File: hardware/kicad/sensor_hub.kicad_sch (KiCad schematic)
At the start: 59 parts, among them J1 5-1634500-1, J2 Wago-DS18B20, J3 Wago-DHT22, J4 Wago-PIR, J5 Wago-GP16, J6 Wago-GP17, J7 Wago-Relay, J8 Phoenix-EC4pin, J9 Phoenix-Power, K1 SRD-05VDC-SL-C, Q1 BC817-40, Q2 BSS84PXUMA1, U1 PicoW, U2 ADS1115IDGSR, U3 LMP91200SD/NOPB, U4 AD8603ARTZ-R2, U5 AP2112K-3.3TRG1, U6 VEML7700-TT

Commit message: hardware: 230 VAC relay spec + sync schematic with docs
- Relays switched to Omron G2RL-1-E (reinforced coil-contact insulation)
  for 230 VAC / 5 A per channel; 8 mm SELV-MAINS creepage/clearance,
  isolation slot, MAINS zone keepout, 3 mm mains traces, X2 snubbers
- Schematic: add K2, Q3, R18, D3, R19/C19, R20/C20, J10 (W7); drop R4
  and second 10M on pH input; renumber pull-ups to one ref per function;
  fix symbol/footprint names for KiCad 10; upgrade file to KiCad 10
- Add project symbol library with VEML7700
- schematic.md gets a master reference designator list; BOM and
  footprints.md aligned; AP2112K fed from VSYS

Co-Authored-By: Claude Opus 5.5 <noreply@anthropic.com>
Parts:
- removed R12, R13, R14: 1k, Resistor_SMD:R_0603_1608Metric, symbol Device:R
- removed R2: 10M, Resistor_SMD:R_0603_1608Metric, symbol Device:R
- removed R22: 10k, Resistor_SMD:R_0603_1608Metric, symbol Device:R
- removed R5, R6: 100k, Resistor_SMD:R_0603_1608Metric, symbol Device:R
- added C19, C20: 100nF X2 275VAC, symbol Device:C
- added D3: 1N4148W, Diode_SMD:D_SOD-123, symbol Device:D
- added J10: Wago-Relay2, symbol Connector_Generic:Conn_01x03
- added K2: G2RL-1-E DC5, Relay_THT:Relay_SPDT_Omron_G2RL-1-E, symbol Relay:G2RL-1-E
- added Q3: BC817-40, Package_TO_SOT_SMD:SOT-23, symbol Transistor_BJT:BC817
- added R18: 1k, Resistor_SMD:R_0603_1608Metric, symbol Device:R
- added R19, R20: 100R, Resistor_SMD:R_1206_3216Metric, symbol Device:R
- J1: footprint Connector_Coaxial:BNC_TE-Connectivity_1-1634500-1_Horizontal -> (none); symbol Connector_Coaxial:BNC_Jack -> Connector:Conn_Coaxial
- J2, J3, J4, J5, J6: footprint TerminalBlock_Wago:TerminalBlock_Wago_2060-453_1x03_P5.00mm_Horizontal -> (none)
- J7: value Wago-Relay -> Wago-Relay1; footprint TerminalBlock_Wago:TerminalBlock_Wago_2060-453_1x03_P5.00mm_Horizontal -> (none)
- J8: footprint TerminalBlock_Phoenix:TerminalBlock_Phoenix_PT-1,5_4-3,5-H_1x04_P3.50mm_Horizontal -> TerminalBlock_Phoenix:TerminalBlock_Phoenix_PT-1,5-4-3.5-H_1x04_P3.50mm_Horizontal
- J9: footprint TerminalBlock_Phoenix:TerminalBlock_Phoenix_PT-1,5_2-5,0-H_1x02_P5.00mm_Horizontal -> TerminalBlock_Phoenix:TerminalBlock_Phoenix_PT-1,5-2-5.0-H_1x02_P5.00mm_Horizontal
- K1: value SRD-05VDC-SL-C -> G2RL-1-E DC5; footprint Relay_THT:Relay_SPDT_Songle_SRD-xxVDC-SL-C -> Relay_THT:Relay_SPDT_Omron_G2RL-1-E; symbol Device:Relay_SPDT -> Relay:G2RL-1-E
- R5: renamed from R19; value 10k -> 4k7
- U1: value PicoW -> Pico W; footprint MicrocontrollerBoard:RaspberryPi_PicoW -> Module:RaspberryPi_Pico_W_SMD; symbol MCU_RaspberryPi_RP2040:RaspberryPi_PicoW -> MCU_Module:RaspberryPi_Pico_W
- U2: footprint Package_SO:VSSOP-10_3x3mm_P0.5mm -> Package_SO:MSOP-10_3x3mm_P0.5mm; symbol Analog_ADC:ADS1115xDGS -> Analog_ADC:ADS1115IDGS
- U3: footprint Package_SO:SOIC-14_3.9x8.65mm_P1.27mm -> Package_SO:SOIC-14_3.9x8.7mm_P1.27mm
- U6: footprint Package_DFN_QFN:DFN-6-1EP_2x2mm_P0.65mm_EP0.7x1.6mm -> (none); symbol Sensor_Optical:VEML7700 -> sensor_hub:VEML7700
- renumbered R3 to R2, R4 to R3, R20 to R6, R21 to R9

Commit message: hardware: restore values/footprints after symbol update, grid-snap and group schematic by block
'Update Symbols from Library' had reset values, footprints and U1/HDR1
references to library defaults; restored from the previous commit by
symbol uuid. All symbols snapped to the 2.54 mm grid so wires land on
pins, grouped into labelled functional blocks, stale notes removed.
U4 footprint follows the KiCad symbol default (TSOT-23-5).

Co-Authored-By: Claude Opus 5.5 <noreply@anthropic.com>
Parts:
- U4: footprint Package_TO_SOT_SMD:SOT-23-5 -> Package_TO_SOT_SMD:TSOT-23-5
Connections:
- new net: U1.13 (GND), U1.18 (GND), U1.23 (GND), U1.28 (GND), U1.3 (GND), U1.38 (GND), U1.8 (GND)
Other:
- note added: "ADC + LIGHT + I2C"
- note added: "MAINS: K1/K2 contacts, R19 C19 R20 C20, J7 (W6), J10 (W7) → netclass MAINS, 8 mm to SELV"
- note added: "MCU + DEBUG"
- note added: "NTC + EC (EC part DNP v1: U3 R15 R16 C3 C4 C5)"
- note added: "POWER (VSYS 5 V in, AP2112K → 3V3_ANA)"
- note added: "RELAY 1 (coil side = SELV)"
- note added: "RELAY 2 (coil side = SELV)"
- note added: "SENSOR PORTS W1–W5 (SELV) + PIR GATE"
- note added: "pH FRONT-END (guard ring on NODE_A, R4 intentionally unused)"
- note removed: "ANALOG ZONE"
- note removed: "After opening: Tools > Update Symbols from Library"
- note removed: "CONNECTORS"
- note removed: "DIGITAL ZONE"
- note removed: "EC ZONE (DNP v1 — AD5933 redesign for v2)"
- note removed: "PIR GATE"
- note removed: "RELAY ZONE"
- note removed: "U3 (LMP91200) + U6 (VEML7700) may need manual symbol search"
- note removed: "Wire per hardware/docs/schematic.md"

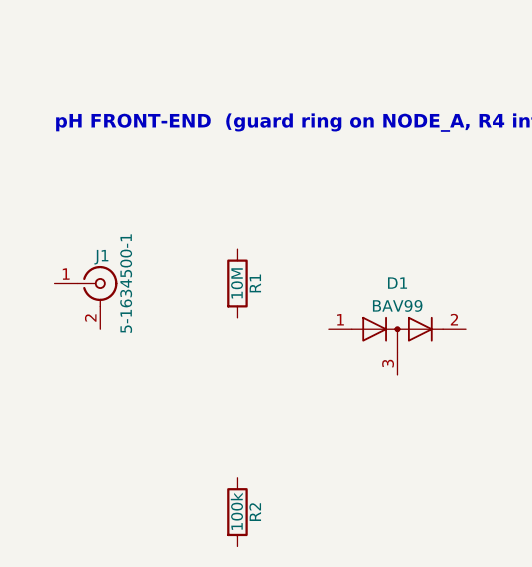
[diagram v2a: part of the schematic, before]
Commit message: hardware: pick library-footprint parts for BNC, Wago ports and X2 snubbers
- J1: Amphenol 031-6575 RA BNC
- J2-J6 (W1-W5): Wago 2601-1103, 3.5 mm
- J7/J10 (W6/W7 mains): Wago 236-403, 24 A IEC / 300 V 15 A UL
- C19/C20: X2 100nF, 13x6 mm body, 10 mm pitch
Only U6 (VEML7700) is still without a footprint.

Co-Authored-By: Claude Opus 5.5 <noreply@anthropic.com>
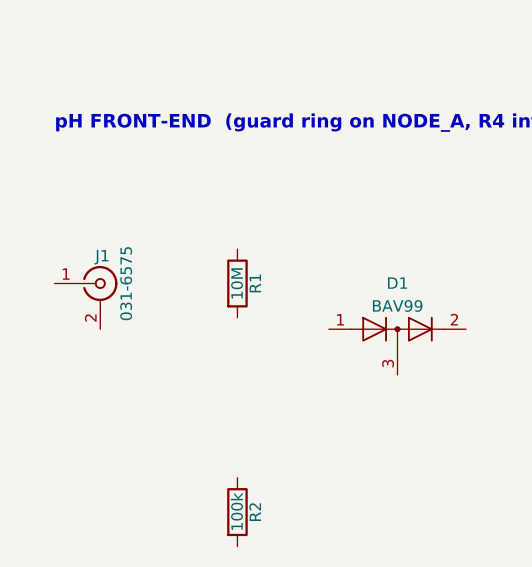
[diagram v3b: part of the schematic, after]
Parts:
- C19, C20: footprint (none) -> Capacitor_THT:C_Rect_L13.0mm_W6.0mm_P10.00mm_FKS3_FKP3_MKS4
- J1: value 5-1634500-1 -> 031-6575; footprint (none) -> Connector_Coaxial:BNC_Amphenol_031-6575_Horizontal
- J10, J7: footprint (none) -> TerminalBlock_WAGO:TerminalBlock_WAGO_236-403_1x03_P5.00mm_45Degree
- J2, J3, J4, J5, J6: footprint (none) -> TerminalBlock_WAGO:TerminalBlock_WAGO_2601-1103_1x03_P3.50mm_Horizontal
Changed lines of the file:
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@@
 			)
 		)
-		(property "Footprint" ""
+		(property "Footprint" "TerminalBlock_WAGO:TerminalBlock_WAGO_2601-1103_1x03_P3.50mm_Horizontal"
 			(at 104.14 243.84 0)
 			(hide yes)
@@
 			)
 		)
-		(property "Footprint" ""
+		(property "Footprint" "TerminalBlock_WAGO:TerminalBlock_WAGO_2601-1103_1x03_P3.50mm_Horizontal"
 			(at 66.04 243.84 0)
 			(hide yes)
@@
 			)
 		)
-		(property "Footprint" ""
+		(property "Footprint" "TerminalBlock_WAGO:TerminalBlock_WAGO_2601-1103_1x03_P3.50mm_Horizontal"
 			(at 205.74 243.84 0)
 			(hide yes)
@@
 			)
 		)
-		(property "Footprint" ""
+		(property "Footprint" "TerminalBlock_WAGO:TerminalBlock_WAGO_236-403_1x03_P5.00mm_45Degree"
 			(at 398.78 68.58 0)
 			(hide yes)
@@
 			)
 		)
-		(property "Value" "5-1634500-1"
+		(property "Value" "031-6575"
 			(at 28.321 88.9 90)
 			(show_name no)
@@
 			)
 		)
-		(property "Footprint" ""
+		(property "Footprint" "Connector_Coaxial:BNC_Amphenol_031-6575_Horizontal"
 			(at 25.4 88.9 0)
 			(hide yes)
@@
 			)
 		)
-		(property "Footprint" ""
+		(property "Footprint" "TerminalBlock_WAGO:TerminalBlock_WAGO_2601-1103_1x03_P3.50mm_Horizontal"
 			(at 175.26 243.84 0)
 			(hide yes)
@@
 			)
 		)
-		(property "Footprint" ""
+		(property "Footprint" "Capacitor_THT:C_Rect_L13.0mm_W6.0mm_P10.00mm_FKS3_FKP3_MKS4"
 			(at 384.5052 54.61 0)
 			(hide yes)
@@
 			)
 		)
-		(property "Footprint" ""
+		(property "Footprint" "TerminalBlock_WAGO:TerminalBlock_WAGO_236-403_1x03_P5.00mm_45Degree"
 			(at 398.78 142.24 0)
 			(hide yes)
@@
 			)
 		)
-		(property "Footprint" ""
+		(property "Footprint" "TerminalBlock_WAGO:TerminalBlock_WAGO_2601-1103_1x03_P3.50mm_Horizontal"
 			(at 25.4 243.84 0)
 			(hide yes)
@@
 			)
 		)
-		(property "Footprint" ""
+		(property "Footprint" "Capacitor_THT:C_Rect_L13.0mm_W6.0mm_P10.00mm_FKS3_FKP3_MKS4"
 			(at 384.5052 128.27 0)
 			(hide yes)

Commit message: hardware: wire the full schematic with net labels
Every pin gets a short stub and a net label (no long wires across the
sheet); unused pins get no-connect flags. Net tie NT1 joins GND_ANA and
GND at the ADS1115, PWR_FLAGs on VSYS and GND_ANA. Netlist verified pin
by pin against docs/schematic.md (197 pins, 0 mismatches). ERC: only the
expected Pico GND/AGND power-output pair. Parts re-spaced so labels do
not overlap. schematic.md: BAV99 pin 3 is the common node.

Co-Authored-By: Claude Opus 5.5 <noreply@anthropic.com>
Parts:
- added NT1: NetTie_2, NetTie:NetTie-2_SMD_Pad0.5mm, symbol Device:NetTie_2
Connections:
- net 3V3_DIG: now reaches R6.1
- net 3V3_DIG: now also C5.1, C9.1, HDR1.4 (Pin_4), J2.1 (Pin_1), J3.1 (Pin_1), J5.1 (Pin_1), J6.1 (Pin_1), Q2.2 (S), R10.1, R11.1, R17.1, R5.1, R9.1, U1.36 (3V3), U6.2 (VDD)
- net DHT_DATA: now reaches R6.2
- net DHT_DATA: now also J3.3 (Pin_3), U1.12 (GPIO9)
- net VSYS: now reaches D3.1 (K)
- net VSYS: now also C10.1, C11.1, C13.1, C14.1, C17.1, C8.1, D2.1 (K), J9.1 (Pin_1), K1.A1, K2.A1, U1.39 (VSYS), U5.1 (VIN), U5.3 (EN)
- net K2_COIL: now reaches D3.2 (A)
- net K2_COIL: now also K2.A2, Q3.3 (C)
- net I2C_SCL: now reaches U6.1 (SCL)
- net I2C_SCL: now also R11.2, U1.5 (GPIO3), U2.10 (SCL)
- net GND: now reaches U6.3 (GND)
- net GND: now also C10.2, C11.2, C13.2, C3.2, C4.2, C5.2, C9.2, HDR1.3 (Pin_3), J2.2 (Pin_2), J3.2 (Pin_2), J4.2 (Pin_2), J5.2 (Pin_2), J6.2 (Pin_2), J9.2 (Pin_2), Q1.2 (E), Q3.2 (E), U1.13 (GND), U1.18 (GND), U1.23 (GND), U1.28 (GND), U1.3 (GND), U1.33 (AGND), U1.38 (GND), U1.8 (GND), NT1.2
- net I2C_SDA: now reaches U6.4 (SDA)
- net I2C_SDA: now also R10.2, U1.4 (GPIO2), U2.9 (SDA)
- net PIR_VCC: now reaches J4.1 (Pin_1)
- net PIR_VCC: now also Q2.3 (D)
- net PIR_OUT: now reaches J4.3 (Pin_3)
- net PIR_OUT: now also R9.2, U1.15 (GPIO11)
- net VREF_MID: now reaches C1.1
- net VREF_MID: now also J1.2 (Ext), R2.2, R3.1
- net GND_ANA: now reaches C1.2
- net GND_ANA: now also C12.2, C14.2, C15.2, C16.2, C17.2, C18.2, C2.2, C6.2, C7.2, C8.2, D1.1 (K), J8.4 (Pin_4), R3.2, U2.1 (ADDR), U2.3 (GND), U4.2 (V-), U5.2 (GND), NT1.1
- net NODE_NTC: now reaches J8.3 (Pin_3)
- net NODE_NTC: now also C6.1, R7.2, U2.5 (AIN1)
- net PIR_EN_N: now reaches R17.2
- net PIR_EN_N: now also Q2.1 (G), U1.16 (GPIO12)
- net W5_SIG: now reaches J6.3 (Pin_3)
- net W5_SIG: now also U1.22 (GPIO17)
- net EC_PWM_A: now reaches R15.1
- net EC_PWM_A: now also U1.17 (GPIO13)
- net EC_EXC_A: now reaches R15.2
- net EC_EXC_A: now also C3.1
- net K1_COM: now reaches J7.1 (Pin_1)
- net K1_COM: now also K1.11, R19.1
- net K1_NO: now reaches J7.2 (Pin_2)
- net K1_NO: now also C19.2, K1.14
- net K1_NC: now reaches J7.3 (Pin_3)
- net K1_NC: now also K1.12
- net PH_BUF: now reaches U2.4 (AIN0)
- net PH_BUF: now also U4.1, U4.4 (-)
- net 3V3_ANA: now reaches U2.8 (VDD)
- net 3V3_ANA: now also C12.1, C15.1, C16.1, C18.1, C2.1, C7.1, D1.2 (A), R2.1, R7.1, U4.5 (V+), U5.5 (VOUT)
- net PH_IN: now reaches J1.1 (In)
- net PH_IN: now also R1.1
- net NODE_A: now reaches D1.3 (K)
- net NODE_A: now also R1.2, U4.3 (+)
- net W4_SIG: now reaches J5.3 (Pin_3)
- net W4_SIG: now also U1.21 (GPIO16)
- net K2_COM: now reaches K2.11
- net K2_COM: now also J10.1 (Pin_1), R20.1
- net K2_NC: now reaches K2.12
- net K2_NC: now also J10.3 (Pin_3)
- net K2_NO: now reaches K2.14
- net K2_NO: now also C20.2, J10.2 (Pin_2)
- net K1_SNUB: now reaches C19.1
- net K1_SNUB: now also R19.2
- net ONEWIRE: now reaches J2.3 (Pin_3)
- net ONEWIRE: now also R5.2, U1.11 (GPIO8)
- net Q1_B: now reaches Q1.1 (B)
- net Q1_B: now also R8.2
- net K1_COIL: now reaches Q1.3 (C)
- net K1_COIL: now also D2.2 (A), K1.A2
- net EC_PWM_B: now reaches R16.1
- net EC_PWM_B: now also U1.19 (GPIO14)
- net EC_EXC_B: now reaches R16.2
- net EC_EXC_B: now also C4.1
- net K2_SNUB: now reaches C20.1
- net K2_SNUB: now also R20.2
- net Q3_B: now reaches Q3.1 (B)
- net Q3_B: now also R18.2
- net RELAY1_DRV: now reaches R8.1
- net RELAY1_DRV: now also U1.14 (GPIO10)
- net RELAY2_DRV: now reaches R18.1
- net RELAY2_DRV: now also U1.20 (GPIO15)
- net UART_TX: now reaches U1.1 (GPIO0)
- net UART_TX: now also HDR1.1 (Pin_1)
- net UART_RX: now reaches U1.2 (GPIO1)
- net UART_RX: now also HDR1.2 (Pin_2)
- no-connect marks 0 -> 22
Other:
- moved on the sheet: C1, C11, C12, C13, C14, C15, C16, C17, C18, C2, C3, C4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

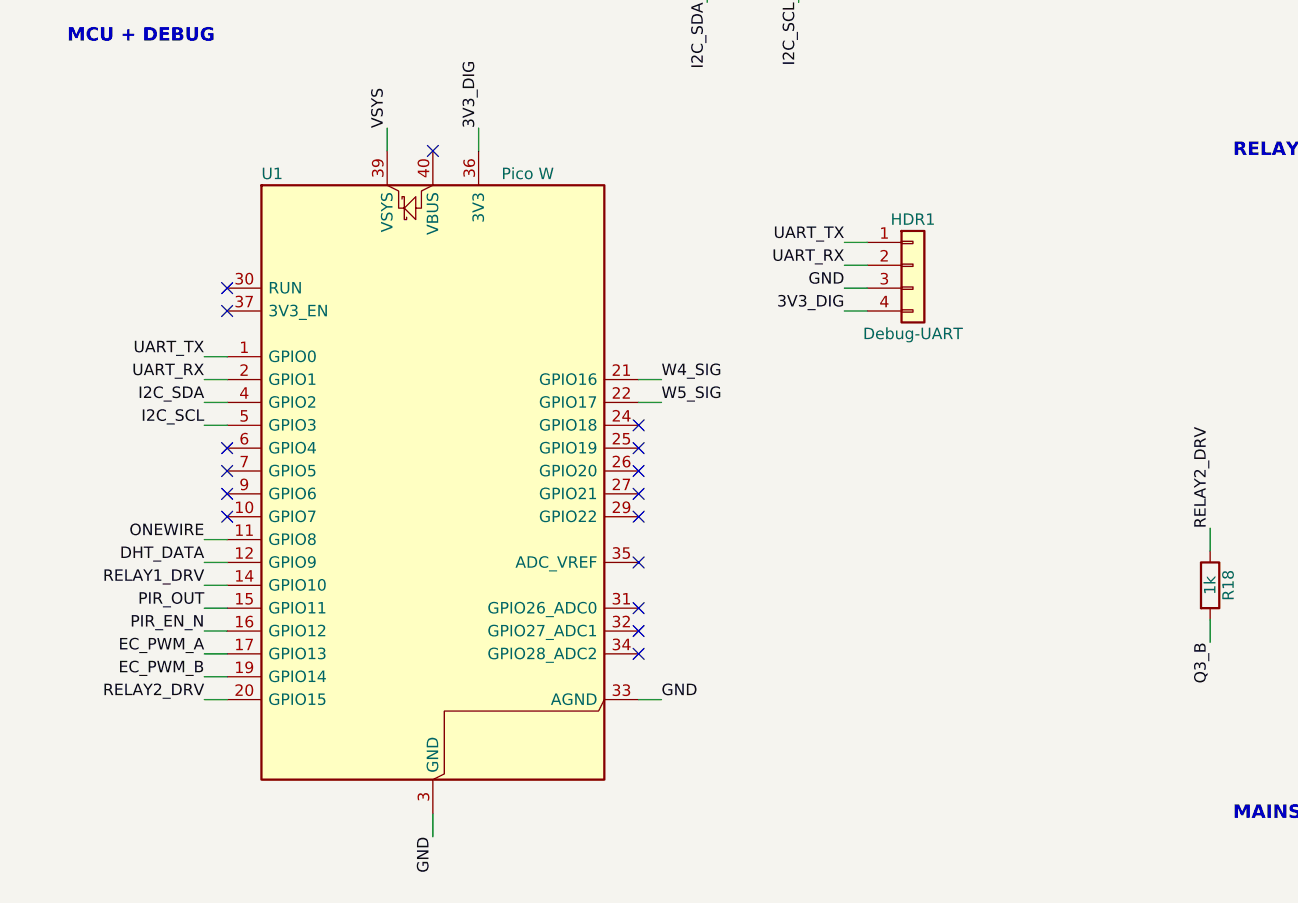
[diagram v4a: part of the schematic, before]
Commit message: hardware: Pico WH on sockets, spare-GPIO breakout J11, VEML7700 footprint
- U1 now uses Module:RaspberryPi_Pico_Common_THT so a Pico WH plugs into
  two 1x20 female headers (added to BOM)
- J11: 2x8 solder-hole breakout (DNP) for GP4-7, GP18-22, GP26-28, RUN,
  3V3_DIG, GND
- Project footprint sensor_hub:VEML7700_TT from Vishay datasheet 84286
  (top-view pad layout, 4 x 0.7x1.6 mm, 1.27 mm pitch); fp-lib-table added
- Netlist re-verified: 213 pins, 0 mismatches

Co-Authored-By: Claude Opus 5.5 <noreply@anthropic.com>
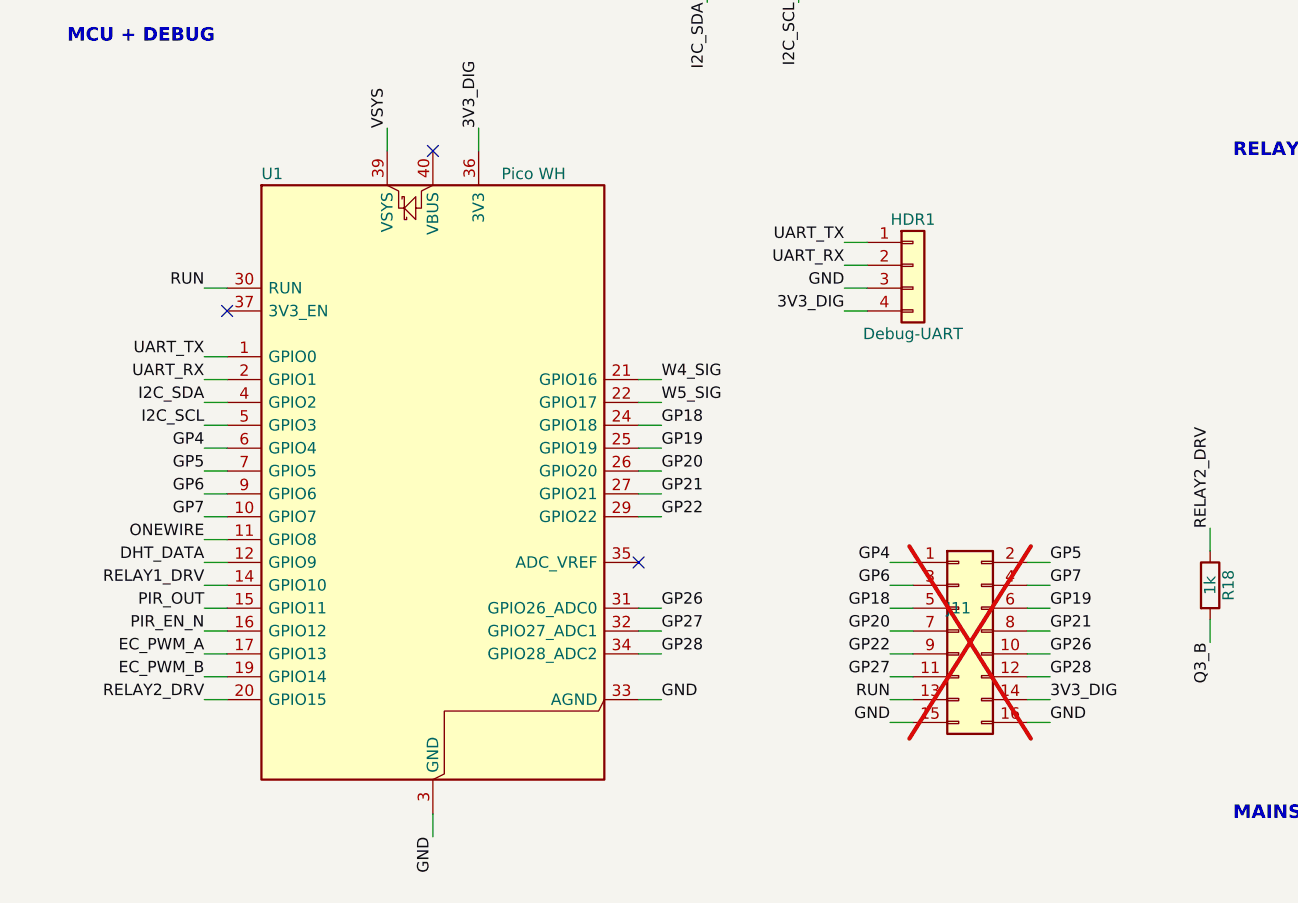
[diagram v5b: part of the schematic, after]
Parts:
- added J11: Spare-GPIO, Connector_PinHeader_2.54mm:PinHeader_2x08_P2.54mm_Vertical, symbol Connector_Generic:Conn_02x08_Odd_Even
- U1: value Pico W -> Pico WH; footprint Module:RaspberryPi_Pico_W_SMD -> Module:RaspberryPi_Pico_Common_THT
- U6: footprint (none) -> sensor_hub:VEML7700_TT
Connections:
- net 3V3_DIG: now also J11.14 (Pin_14)
- net GND: now also J11.15 (Pin_15), J11.16 (Pin_16)
- net GP7: now reaches U1.10 (GPIO7)
- net GP7: now also J11.4 (Pin_4)
- net GP18: now reaches U1.24 (GPIO18)
- net GP18: now also J11.5 (Pin_5)
- net GP19: now reaches U1.25 (GPIO19)
- net GP19: now also J11.6 (Pin_6)
- net GP20: now reaches U1.26 (GPIO20)
- net GP20: now also J11.7 (Pin_7)
- net GP21: now reaches U1.27 (GPIO21)
- net GP21: now also J11.8 (Pin_8)
- net GP22: now reaches U1.29 (GPIO22)
- net GP22: now also J11.9 (Pin_9)
- net RUN: now reaches U1.30 (RUN)
- net RUN: now also J11.13 (Pin_13)
- net GP26: now reaches U1.31 (GPIO26_ADC0)
- net GP26: now also J11.10 (Pin_10)
- net GP27: now reaches U1.32 (GPIO27_ADC1)
- net GP27: now also J11.11 (Pin_11)
- net GP28: now reaches U1.34 (GPIO28_ADC2)
- net GP28: now also J11.12 (Pin_12)
- net GP4: now reaches U1.6 (GPIO4)
- net GP4: now also J11.1 (Pin_1)
- net GP5: now reaches U1.7 (GPIO5)
- net GP5: now also J11.2 (Pin_2)
- net GP6: now reaches U1.9 (GPIO6)
- net GP6: now also J11.3 (Pin_3)
- no-connect marks 22 -> 9

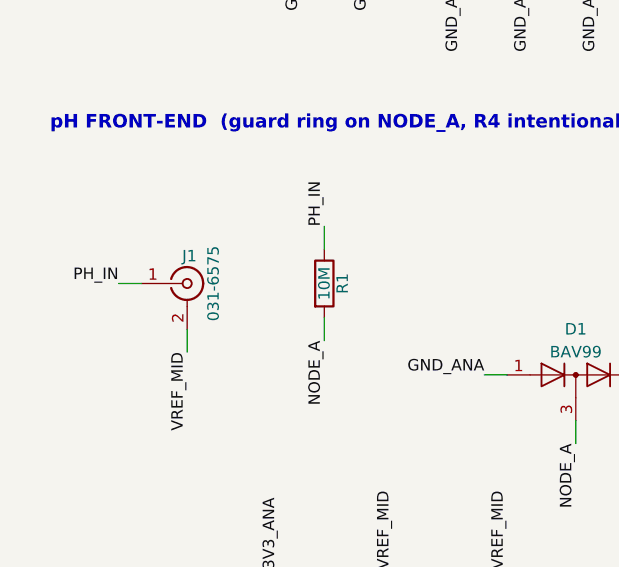
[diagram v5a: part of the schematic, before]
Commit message: hardware: first board placement, outline and 230 VAC design rules
- Board 100 x 100 mm (fits 8 mm MAINS separation + socketed Pico WH),
  4x M3 holes (board-only), 2 mm isolation slots: under the relays
  (coil | contacts) and along the MAINS zone boundary
- Zone placement: power + ADC + pH top/left (BNC at left edge), Pico WH
  centre (USB at top), relays + W6/W7 + snubbers in MAINS zone top right,
  sensor ports along the bottom edge
- Net classes (Default/Power/VSYS/MAINS) and sensor_hub.kicad_dru:
  MAINS<->SELV 8 mm clearance/creepage/hole clearance, K1<->K2 4 mm
- Rule areas: MAINS (no pour/vias), pH high-Z (no pour), Pico W antenna
- J1 changed to TE 1-1478035-0 (all shield pads = pad 2)
- DRC: 0 clearance/creepage/courtyard errors, schematic parity clean;
  only unrouted nets and silkscreen cosmetics remain

Co-Authored-By: Claude Opus 5.5 <noreply@anthropic.com>
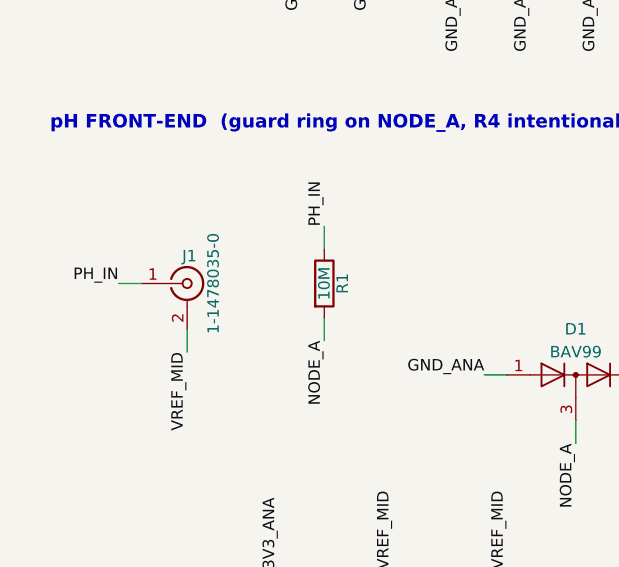
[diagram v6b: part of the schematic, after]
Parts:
- J1: value 031-6575 -> 1-1478035-0; footprint Connector_Coaxial:BNC_Amphenol_031-6575_Horizontal -> Connector_Coaxial:BNC_TEConnectivity_1478035_Horizontal
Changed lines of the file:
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@@
 			)
 		)
-		(property "Value" "031-6575"
+		(property "Value" "1-1478035-0"
 			(at 38.481 88.9 90)
 			(show_name no)
@@
 			)
 		)
-		(property "Footprint" "Connector_Coaxial:BNC_Amphenol_031-6575_Horizontal"
+		(property "Footprint" "Connector_Coaxial:BNC_TEConnectivity_1478035_Horizontal"
 			(at 35.56 88.9 0)
 			(hide yes)
